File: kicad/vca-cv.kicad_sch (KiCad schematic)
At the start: 11 parts, among them Q14 2N3906, U19 TL072

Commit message: geographically reannotate parts
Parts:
- renumbered C58 to C41, C59 to C45, C57 to C46, D40 to D13, Q14 to Q7, R57 to R110, R135 to R72, R133 to R73, R134 to R74, R136 to R94, U19 to U9
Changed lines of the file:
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@@
   (symbol (lib_id "rumblesan-standard-parts:C") (at 133.35 83.82 90) (unit 1)
     (in_bom yes) (on_board yes) (fields_autoplaced)
-    (property "Reference" "C57" (id 0) (at 133.35 77.9612 90))
+    (property "Reference" "C46" (id 0) (at 133.35 77.9612 90))
     (property "Value" "220pF" (id 1) (at 133.35 80.4981 90))
     (property "Footprint" "rumblesan-standard-parts:C_Rect_L7.0mm_W2.5mm_P5.00mm" (id 2) (at 132.08 78.105 0)
@@
   (symbol (lib_id "Amplifier_Operational:TL072") (at 133.35 97.79 0) (mirror x) (unit 1)
     (in_bom yes) (on_board yes) (fields_autoplaced)
-    (property "Reference" "U19" (id 0) (at 133.35 89.0102 0))
+    (property "Reference" "U9" (id 0) (at 133.35 89.0102 0))
     (property "Value" "TL072" (id 1) (at 133.35 91.5471 0))
     (property "Footprint" "rumblesan-standard-parts:DIP-8_W7.62mm_Socket" (id 2) (at 133.35 97.79 0)
@@
   (symbol (lib_id "rumblesan-standard-parts:R") (at 138.43 64.77 90) (unit 1)
     (in_bom yes) (on_board yes) (fields_autoplaced)
-    (property "Reference" "R136" (id 0) (at 138.43 60.0542 90))
+    (property "Reference" "R94" (id 0) (at 138.43 60.0542 90))
     (property "Value" "33k" (id 1) (at 138.43 62.5911 90))
     (property "Footprint" "rumblesan-standard-parts:R_Axial_DIN0207_L6.3mm_D2.5mm_P10.16mm_Horizontal" (id 2) (at 140.97 62.23 90)
@@
   (symbol (lib_id "rumblesan-standard-parts:R") (at 166.37 64.77 90) (unit 1)
     (in_bom yes) (on_board yes) (fields_autoplaced)
-    (property "Reference" "R57" (id 0) (at 166.37 60.0542 90))
+    (property "Reference" "R110" (id 0) (at 166.37 60.0542 90))
     (property "Value" "1k" (id 1) (at 166.37 62.5911 90))
     (property "Footprint" "rumblesan-standard-parts:R_Axial_DIN0207_L6.3mm_D2.5mm_P10.16mm_Horizontal" (id 2) (at 168.91 62.23 90)
@@
   (symbol (lib_id "rumblesan-standard-parts:R") (at 109.22 74.93 90) (unit 1)
     (in_bom yes) (on_board yes) (fields_autoplaced)
-    (property "Reference" "R134" (id 0) (at 109.22 70.2142 90))
+    (property "Reference" "R74" (id 0) (at 109.22 70.2142 90))
     (property "Value" "100k" (id 1) (at 109.22 72.7511 90))
     (property "Footprint" "rumblesan-standard-parts:R_Axial_DIN0207_L6.3mm_D2.5mm_P10.16mm_Horizontal" (id 2) (at 111.76 72.39 90)
@@
   (symbol (lib_id "Device:D") (at 133.35 73.66 0) (unit 1)
     (in_bom yes) (on_board yes) (fields_autoplaced)
-    (property "Reference" "D40" (id 0) (at 133.35 68.6902 0))
+    (property "Reference" "D13" (id 0) (at 133.35 68.6902 0))
     (property "Value" "1n4148" (id 1) (at 133.35 71.2271 0))
     (property "Footprint" "rumblesan-standard-parts:D_DO-35_SOD27_P7.62mm_Horizontal" (id 2) (at 133.35 73.66 0)
@@
   (symbol (lib_id "Amplifier_Operational:TL072") (at 92.71 74.93 0) (mirror x) (unit 2)
     (in_bom yes) (on_board yes) (fields_autoplaced)
-    (property "Reference" "U19" (id 0) (at 92.71 66.1502 0))
+    (property "Reference" "U9" (id 0) (at 92.71 66.1502 0))
     (property "Value" "TL072" (id 1) (at 92.71 68.6871 0))
     (property "Footprint" "rumblesan-standard-parts:DIP-8_W7.62mm_Socket" (id 2) (at 92.71 74.93 0)
@@
   (symbol (lib_id "Amplifier_Operational:TL072") (at 203.2 68.58 0) (unit 3)
     (in_bom yes) (on_board yes)
-    (property "Reference" "U19" (id 0) (at 194.31 67.31 0)
+    (property "Reference" "U9" (id 0) (at 194.31 67.31 0)
       (effects (font (size 1.27 1.27)) (justify left))
     )
@@
   (symbol (lib_id "rumblesan-standard-parts:R") (at 110.49 95.25 90) (unit 1)
     (in_bom yes) (on_board yes) (fields_autoplaced)
-    (property "Reference" "R135" (id 0) (at 110.49 90.5342 90))
+    (property "Reference" "R72" (id 0) (at 110.49 90.5342 90))
     (property "Value" "330k" (id 1) (at 110.49 93.0711 90))
     (property "Footprint" "rumblesan-standard-parts:R_Axial_DIN0207_L6.3mm_D2.5mm_P10.16mm_Horizontal" (id 2) (at 113.03 92.71 90)
@@
   (symbol (lib_id "Transistor_BJT:2N3906") (at 151.13 97.79 0) (mirror x) (unit 1)
     (in_bom yes) (on_board yes) (fields_autoplaced)
-    (property "Reference" "Q14" (id 0) (at 155.9814 96.9553 0)
+    (property "Reference" "Q7" (id 0) (at 155.9814 96.9553 0)
       (effects (font (size 1.27 1.27)) (justify left))
     )
@@
   (symbol (lib_id "rumblesan-standard-parts:C") (at 209.55 62.23 0) (unit 1)
     (in_bom yes) (on_board yes) (fields_autoplaced)
-    (property "Reference" "C58" (id 0) (at 212.471 61.3953 0)
+    (property "Reference" "C41" (id 0) (at 212.471 61.3953 0)
       (effects (font (size 1.27 1.27)) (justify left))
     )
@@
   (symbol (lib_id "rumblesan-standard-parts:R") (at 92.71 59.69 90) (unit 1)
     (in_bom yes) (on_board yes) (fields_autoplaced)
-    (property "Reference" "R133" (id 0) (at 92.71 54.9742 90))
+    (property "Reference" "R73" (id 0) (at 92.71 54.9742 90))
     (property "Value" "100k" (id 1) (at 92.71 57.5111 90))
     (property "Footprint" "rumblesan-standard-parts:R_Axial_DIN0207_L6.3mm_D2.5mm_P10.16mm_Horizontal" (id 2) (at 95.25 57.15 90)
@@
   (symbol (lib_id "rumblesan-standard-parts:C") (at 209.55 74.93 0) (unit 1)
     (in_bom yes) (on_board yes) (fields_autoplaced)
-    (property "Reference" "C59" (id 0) (at 212.471 74.0953 0)
-      (effects (font (size 1.27 1.27)) (justify left))
-    )
+    (property "Reference" "C45" (id 0) (at 212.471 74.0953 0)
+      (effects (font (size 1.27 1.27)) (justify left))
+    )

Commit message: Changing name again
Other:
- title: The Mercurial Machine -> Ouroboros
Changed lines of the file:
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@@
   (paper "A4")
   (title_block
-    (title "The Mercurial Machine")
+    (title "Ouroboros")
     (date "2023-05-13")
     (rev "r02")

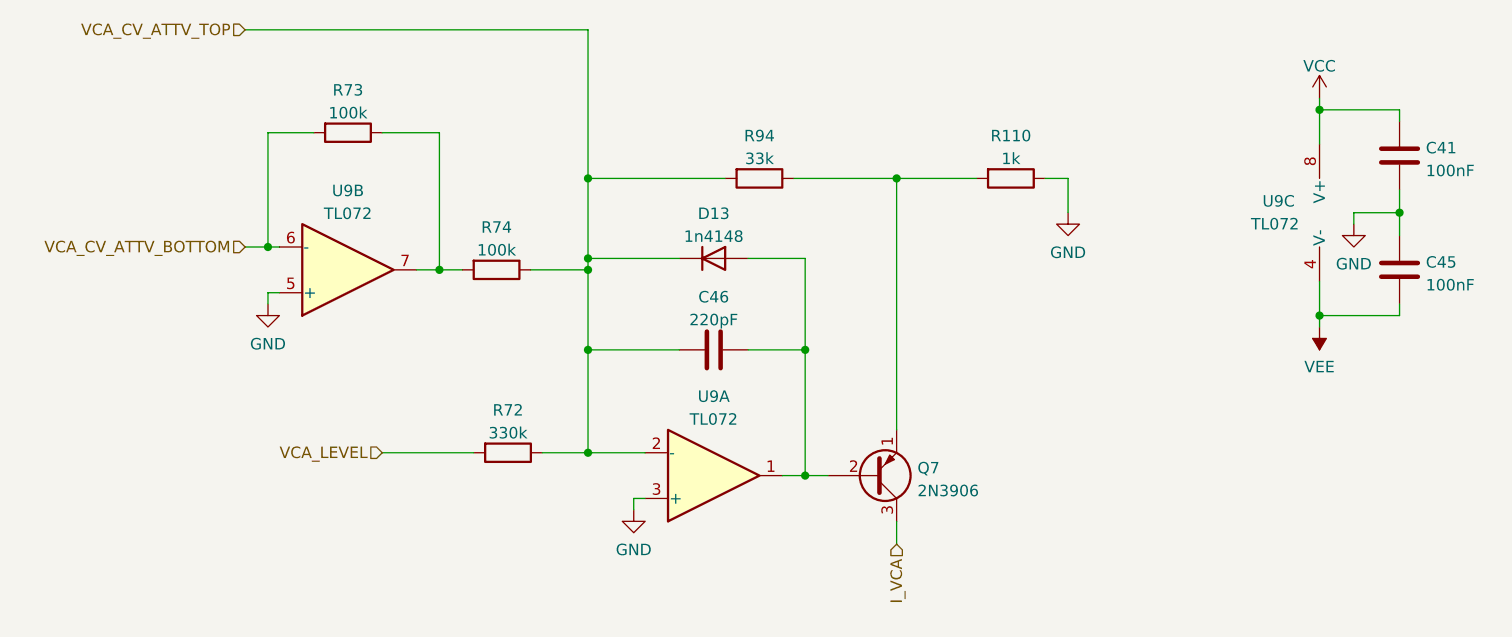
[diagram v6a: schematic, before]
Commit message: Updating for kicad 7
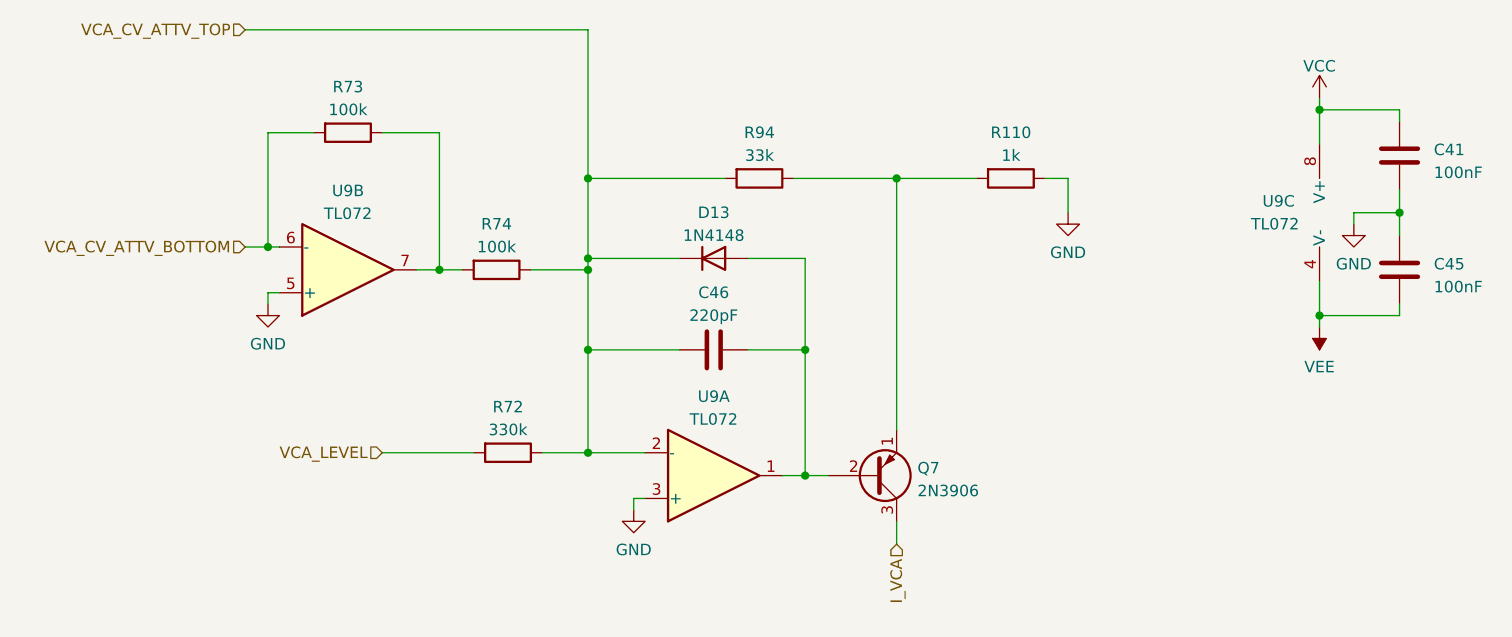
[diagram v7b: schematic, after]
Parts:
- C41, C45: footprint rumblesan-standard-parts:C_Rect_L7.0mm_W2.5mm_P5.00mm -> Rumblesan_Standard_Parts:C_Rect_L7.0mm_W2.5mm_P5.00mm; symbol rumblesan-standard-parts:C -> Rumblesan Standard Parts:C; Spec ceramic X7R -> ceramic C0G
- C46: footprint rumblesan-standard-parts:C_Rect_L7.0mm_W2.5mm_P5.00mm -> Rumblesan_Standard_Parts:C_Rect_L7.0mm_W2.5mm_P5.00mm; symbol rumblesan-standard-parts:C -> Rumblesan Standard Parts:C
- D13: value 1n4148 -> 1N4148; footprint rumblesan-standard-parts:D_DO-35_SOD27_P7.62mm_Horizontal -> Rumblesan_Standard_Parts:D_DO-35_SOD27_P7.62mm_Horizontal
- Q7: footprint rumblesan-standard-parts:TO-92_Inline_Wide -> Rumblesan_Standard_Parts:TO-92_Inline_Wide
- R110, R72, R73, R74, R94: footprint rumblesan-standard-parts:R_Axial_DIN0207_L6.3mm_D2.5mm_P10.16mm_Horizontal -> Rumblesan_Standard_Parts:R_Axial_DIN0207_L6.3mm_D2.5mm_P10.16mm_Horizontal; symbol rumblesan-standard-parts:R -> Rumblesan Standard Parts:R
- U9: footprint rumblesan-standard-parts:DIP-8_W7.62mm_Socket -> Rumblesan_Standard_Parts:DIP-8_W7.62mm_Socket

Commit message: Changing decoupling caps to ceramic X7R
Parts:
- C41, C45: Spec ceramic C0G -> ceramic X7R
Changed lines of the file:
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@@
       (effects (font (size 1.27 1.27)) hide)
     )
-    (property "Spec" "ceramic C0G" (at 213.36 62.23 90)
+    (property "Spec" "ceramic X7R" (at 213.36 62.23 90)
       (effects (font (size 1.27 1.27)) hide)
     )
@@
       (effects (font (size 1.27 1.27)) hide)
     )
-    (property "Spec" "ceramic C0G" (at 213.36 74.93 90)
+    (property "Spec" "ceramic X7R" (at 213.36 74.93 90)
       (effects (font (size 1.27 1.27)) hide)
     )
